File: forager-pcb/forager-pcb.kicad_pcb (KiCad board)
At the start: 2 copper layers, 272.5 x 96.3 mm, 102 parts, among them J1 Conn_01x02_Pin, J2 Conn_01x02_Pin

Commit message: Move out components to edges and clear all traces
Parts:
- moved LCH1 18.0 mm to (-125.0, -28.0)
- moved LCH13 18.0 mm to (-125.0, 6.00)
- moved LCH7 18.0 mm to (-125.0, -11.0)
- moved LU1 18.0 mm to (-125.5, -40.0)
- moved RCH12 18.0 mm to (125.0, -11.0)
- moved RCH18 18.0 mm to (125.0, 6.00)
- moved RCH6 18.0 mm to (125.0, -28.0)
- moved REF** 18.0 mm to (-111.2, -45.8)
- moved REF** 18.0 mm to (111.2, -45.8)
- moved RU1 18.0 mm to (125.5, -40.0)
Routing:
- net /LROW3: track 159.1 -> 0.00 mm
- net /RCOL4: track 156.1 -> 0.00 mm, vias 1 -> 0
- net /LCOL4: track 153.3 -> 0.00 mm, vias 1 -> 0
- net /LROW1: track 136.9 -> 0.00 mm
- net /RCOL3: track 135.8 -> 0.00 mm, vias 1 -> 0
- net /LCOL3: track 133.6 -> 0.00 mm, vias 1 -> 0
- net /RROW2: track 113.4 -> 0.00 mm
- net /RROW3: track 110.5 -> 0.00 mm
- net /LCOL2: track 97.2 -> 0.00 mm, vias 1 -> 0
- net Net-(LD7-A): track 91.4 -> 0.00 mm
- net LBAT: track 90.7 -> 0.00 mm
- net /LROW2: track 84.9 -> 0.00 mm, vias 2 -> 0
- net RBAT: track 83.9 -> 0.00 mm
- net /LCOL1: track 82.1 -> 0.00 mm, vias 1 -> 0
- net /RCOL2: track 76.3 -> 0.00 mm, vias 1 -> 0
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
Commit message: Move in new columns
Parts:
- moved RCH11 124.3 mm to (107.0, -14.6)
- moved RCH17 124.3 mm to (107.0, 1.72)
- moved RCH5 124.3 mm to (107.0, -31.0)
- moved LCH14 122.4 mm to (-107.0, 1.77)
- moved LCH2 122.4 mm to (-107.0, -30.9)
- moved LCH8 122.4 mm to (-107.0, -14.6)
- moved LD14 32.2 mm to (-46.4, 78.2)
- moved LD2 32.2 mm to (-46.4, 71.5)
- moved LD8 32.2 mm to (-46.4, 74.8)
- moved LCH15 1.00 mm to (-89.0, -1.00)
- moved LCH3 1.00 mm to (-89.0, -35.0)
- moved LCH9 1.00 mm to (-89.0, -18.0)
- moved RCH10 1.00 mm to (89.0, -18.0)
- moved RCH16 1.00 mm to (89.0, -1.00)
- moved RCH4 1.00 mm to (89.0, -35.0)
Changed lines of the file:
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@@
 	(footprint "Custom:SW_choc_v1_HS_MBK"
 		(layer "B.Cu")
-		(at 44 92.56 180)
+		(at 107 -14.64 180)
 		(descr "Hotswap footprint for Kailh Choc style switches")
 		(property "Reference" "RCH11"
@@
 	(footprint "Custom:SW_choc_v1_HS_MBK"
 		(layer "B.Cu")
-		(at -89 -34)
+		(at -89 -35)
 		(descr "Hotswap footprint for Kailh Choc style switches")
 		(property "Reference" "LCH3"
@@
 	(footprint "Custom:SW_choc_v1_HS_MBK"
 		(layer "B.Cu")
-		(at -89 -17 180)
+		(at -89 -18 180)
 		(descr "Hotswap footprint for Kailh Choc style switches")
 		(property "Reference" "LCH9"
@@
 	(footprint "Custom:SW_choc_v1_HS_MBK"
 		(layer "B.Cu")
-		(at 89 0)
+		(at 89 -1)
 		(descr "Hotswap footprint for Kailh Choc style switches")
 		(property "Reference" "RCH16"
@@
 	(footprint "Custom:SW_choc_v1_HS_MBK"
 		(layer "B.Cu")
-		(at 89 -17 180)
+		(at 89 -18 180)
 		(descr "Hotswap footprint for Kailh Choc style switches")
 		(property "Reference" "RCH10"
@@
 	(footprint "Diode_SMD:D_SOD-123"
 		(layer "B.Cu")
-		(at -14.35 71.5 180)
+		(at -46.35 74.85 180)
 		(descr "SOD-123")
 		(tags "SOD-123")
@@
 	(footprint "Diode_SMD:D_SOD-123"
 		(layer "B.Cu")
-		(at -14.35 74.85 180)
+		(at -46.35 78.2 180)
 		(descr "SOD-123")
 		(tags "SOD-123")
@@
 	(footprint "Custom:SW_choc_v1_HS_MBK"
 		(layer "B.Cu")
-		(at -89 0)
+		(at -89 -1)
 		(descr "Hotswap footprint for Kailh Choc style switches")
 		(property "Reference" "LCH15"
@@
 	(footprint "Custom:SW_choc_v1_HS_MBK"
 		(layer "B.Cu")
-		(at -33.5 83.28 180)
+		(at -107 -14.59 180)
 		(descr "Hotswap footprint for Kailh Choc style switches")
 		(property "Reference" "LCH8"
@@
 	(footprint "Custom:SW_choc_v1_HS_MBK"
 		(layer "B.Cu")
-		(at -33.5 66.92 180)
+		(at -107 -30.95 180)
 		(descr "Hotswap footprint for Kailh Choc style switches")
 		(property "Reference" "LCH2"
@@
 	(footprint "Custom:SW_choc_v1_HS_MBK"
 		(layer "B.Cu")
-		(at 89 -34 180)
+		(at 89 -35 180)
 		(descr "Hotswap footprint for Kailh Choc style switches")
 		(property "Reference" "RCH4"
@@
 	(footprint "Custom:SW_choc_v1_HS_MBK"
 		(layer "B.Cu")
-		(at -33.5 99.64 180)
+		(at -107 1.77 180)
 		(descr "Hotswap footprint for Kailh Choc style switches")
 		(property "Reference" "LCH14"
@@
 	(footprint "Diode_SMD:D_SOD-123"
 		(layer "B.Cu")
-		(at -14.35 68.15 180)
+		(at -46.35 71.5 180)
 		(descr "SOD-123")
 		(tags "SOD-123")
@@
 	(footprint "Custom:SW_choc_v1_HS_MBK"
 		(layer "B.Cu")
-		(at 44 76.2 180)
+		(at 107 -31 180)
 		(descr "Hotswap footprint for Kailh Choc style switches")
 		(property "Reference" "RCH5"
@@
 	(footprint "Custom:SW_choc_v1_HS_MBK"
 		(layer "B.Cu")
-		(at 44 108.92 180)
+		(at 107 1.72 180)
 		(descr "Hotswap footprint for Kailh Choc style switches")
 		(property "Reference" "RCH17"

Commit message: Set left diodes
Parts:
- moved LD2 117.6 mm to (-50.0, -46.0), turned to -90 degrees
- moved LD8 97.9 mm to (-22.0, -20.0)
- moved LD14 75.8 mm to (-85.0, 13.0), turned to 90 degrees
- moved LD10 3.00 mm to (-22.0, -14.0)
- moved LD11 3.00 mm to (-22.0, -11.0)
- moved LD12 3.00 mm to (-22.0, -8.00)
- moved LD15 3.00 mm to (-82.0, 13.0)
- moved LD3 3.00 mm to (-53.0, -46.0)
- moved LD4 3.00 mm to (-56.0, -46.0)
- moved LD9 3.00 mm to (-22.0, -17.0)
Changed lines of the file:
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@@
 	(footprint "Diode_SMD:D_SOD-123"
 		(layer "B.Cu")
-		(at -85 13 90)
+		(at -82 13 90)
 		(descr "SOD-123")
 		(tags "SOD-123")
@@
 			(at 0 2 0)
 			(layer "B.SilkS")
+			(hide yes)
 			(effects
 				(font
@@
 			(at 0 2 0)
 			(layer "B.SilkS")
+			(hide yes)
 			(effects
 				(font
@@
 	(footprint "Diode_SMD:D_SOD-123"
 		(layer "B.Cu")
-		(at -22 -14 180)
+		(at -22 -11 180)
 		(descr "SOD-123")
 		(tags "SOD-123")
@@
 			(at 0 2 0)
 			(layer "B.SilkS")
+			(hide yes)
 			(effects
 				(font
@@
 	(footprint "Diode_SMD:D_SOD-123"
 		(layer "B.Cu")
-		(at -46.35 74.85 180)
+		(at -22 -20 180)
 		(descr "SOD-123")
 		(tags "SOD-123")
@@
 			(at 0 2 0)
 			(layer "B.SilkS")
+			(hide yes)
 			(effects
 				(font
@@
 	(footprint "Diode_SMD:D_SOD-123"
 		(layer "B.Cu")
-		(at -22 -20 180)
+		(at -22 -17 180)
 		(descr "SOD-123")
 		(tags "SOD-123")
@@
 	(footprint "Diode_SMD:D_SOD-123"
 		(layer "B.Cu")
-		(at -46.35 78.2 180)
+		(at -85 13 90)
 		(descr "SOD-123")
 		(tags "SOD-123")
 		(property "Reference" "LD14"
-			(at 0 2 0)
+			(at 0 2 90)
 			(layer "B.SilkS")
+			(hide yes)
 			(effects
 				(font
@@
 		)
 		(property "Value" "D"
-			(at 0 -2.1 0)
+			(at 0 -2.1 90)
 			(layer "B.Fab")
 			(effects
@@
 		)
 		(property "Footprint" "Diode_SMD:D_SOD-123"
-			(at 0 0 0)
+			(at 0 0 -90)
 			(unlocked yes)
 			(layer "B.Fab")
@@
 		)
 		(property "Datasheet" ""
-			(at 0 0 0)
+			(at 0 0 -90)
 			(unlocked yes)
 			(layer "B.Fab")
@@
 		)
 		(property "Description" "Diode"
-			(at 0 0 0)
+			(at 0 0 -90)
 			(unlocked yes)
 			(layer "B.Fab")
@@
 		)
 		(property "Sim.Device" "D"
-			(at 0 0 0)
+			(at 0 0 -90)
 			(unlocked yes)
 			(layer "B.Fab")
@@
 		)
 		(property "Sim.Pins" "1=K 2=A"
-			(at 0 0 0)
+			(at 0 0 -90)
 			(unlocked yes)
 			(layer "B.Fab")
@@
 		(attr smd)
 		(fp_line
-			(start 1.65 1)
-			(end -2.36 1)
-			(stroke
-				(width 0.12)
-				(type solid)
-			)
-			(layer "B.SilkS")
-		)
-		(fp_line
 			(start 1.65 -1)
 			(end -2.36 -1)
@@
 		)
 		(fp_line
-			(start 2.35 1.15)
-			(end -2.35 1.15)
+			(start 1.65 1)
+			(end -2.36 1)
 			(stroke
-				(width 0.05)
+				(width 0.12)
 				(type solid)
 			)
-			(layer "B.CrtYd")
+			(layer "B.SilkS")
 		)
 		(fp_line
@@
 		)
 		(fp_line
-			(start 1.4 0.9)
-			(end -1.4 0.9)
+			(start 2.35 1.15)
+			(end -2.35 1.15)
 			(stroke
-				(width 0.1)
+				(width 0.05)
 				(type solid)
 			)
-			(layer "B.Fab")
+			(layer "B.CrtYd")
 		)
 		(fp_line
@@
 		)
 		(fp_line
-			(start 0.75 0)
-			(end 0.25 0)
+			(start -1.4 -0.9)
+			(end 1.4 -0.9)
 			(stroke
 				(width 0.1)
@@
 		)
 		(fp_line
-			(start 0.25 0.4)
+			(start -0.35 -0.55)
 			(end -0.35 0)
 			(stroke
@@
 		)
 		(fp_line
-			(start -0.35 0.55)
-			(end -0.35 0)
+			(start 0.75 0)
+			(end 0.25 0)
 			(stroke
 				(width 0.1)
@@
 		)
 		(fp_line
-			(start -0.35 -0.55)
+			(start 0.25 0.4)
 			(end -0.35 0)
 			(stroke
@@
 		)
 		(fp_line
-			(start -1.4 0.9)
-			(end -1.4 -0.9)
+			(start -0.35 0.55)
+			(end -0.35 0)
 			(stroke
 				(width 0.1)
@@
 		)
 		(fp_line
-			(start -1.4 -0.9)
-			(end 1.4 -0.9)
+			(start 1.4 0.9)
+			(end -1.4 0.9)
+			(stroke
+				(width 0.1)
+				(type solid)
+			)
+			(layer "B.Fab")
+		)
+		(fp_line
+			(start -1.4 0.9)
+			(end -1.4 -0.9)
 			(stroke
 				(width 0.1)
@@
 		)
 		(fp_text user "${REFERENCE}"
-			(at 0 2 0)
+			(at 0 2 90)
 			(layer "B.Fab")
 			(effects
@@
 		)
 		(pad "1" smd roundrect
-			(at -1.65 0 180)
+			(at -1.65 0 90)
 			(size 0.9 1.2)
 			(layers "B.Cu" "B.Paste" "B.Mask")
@@
 		)
 		(pad "2" smd roundrect
-			(at 1.65 0 180)
+			(at 1.65 0 90)
 			(size 0.9 1.2)
 			(layers "B.Cu" "B.Paste" "B.Mask")
@@
 	(footprint "Diode_SMD:D_SOD-123"
 		(layer "B.Cu")
-		(at -50 -46 -90)
+		(at -53 -46 -90)
 		(descr "SOD-123")
 		(tags "SOD-123")
@@
 	(footprint "Diode_SMD:D_SOD-123"
 		(layer "B.Cu")
-		(at -22 -17 180)
+		(at -22 -14 180)
 		(descr "SOD-123")
 		(tags "SOD-123")
@@
 	(footprint "Diode_SMD:D_SOD-123"
 		(layer "B.Cu")
-		(at -46.35 71.5 180)
+		(at -50 -46 -90)
 		(descr "SOD-123")
 		(tags "SOD-123")
 		(property "Reference" "LD2"
-			(at 0 2 0)
+			(at 0 2 90)
 			(layer "B.SilkS")
+			(hide yes)
 			(effects
 				(font
@@
 		)
 		(property "Value" "D"
-			(at 0 -2.1 0)
+			(at 0 -2.1 90)
 			(layer "B.Fab")
 			(effects
@@
 		)
 		(property "Footprint" "Diode_SMD:D_SOD-123"
-			(at 0 0 0)
+			(at 0 0 90)
 			(unlocked yes)
 			(layer "B.Fab")
@@
 		)
 		(property "Datasheet" ""
-			(at 0 0 0)
+			(at 0 0 90)
 			(unlocked yes)
 			(layer "B.Fab")
@@
 		)
 		(property "Description" "Diode"
-			(at 0 0 0)
+			(at 0 0 90)
 			(unlocked yes)
 			(layer "B.Fab")
@@
 		)
 		(property "Sim.Device" "D"
-			(at 0 0 0)
+			(at 0 0 90)
 			(unlocked yes)
 			(layer "B.Fab")
@@
 		)
 		(property "Sim.Pins" "1=K 2=A"
-			(at 0 0 0)
+			(at 0 0 90)
 			(unlocked yes)
 			(layer "B.Fab")
@@
 		)
 		(fp_line
-			(start 1.65 -1)
-			(end -2.36 -1)
+			(start -2.36 -1)
+			(end -2.36 1)
 			(stroke
 				(width 0.12)
@@
 		)
 		(fp_line
-			(start -2.36 -1)
-			(end -2.36 1)
+			(start 1.65 -1)
+			(end -2.36 -1)
 			(stroke
 				(width 0.12)
@@
 		)
 		(fp_line
-			(start 2.35 -1.15)
-			(end 2.35 1.15)
+			(start -2.35 -1.15)
+			(end -2.35 1.15)
 			(stroke
 				(width 0.05)
@@
 		)
 		(fp_line
-			(start -2.35 -1.15)
-			(end -2.35 1.15)
+			(start 2.35 -1.15)
+			(end 2.35 1.15)
 			(stroke
 				(width 0.05)
@@
 		)
 		(fp_line
-			(start 1.4 0.9)
-			(end -1.4 0.9)
+			(start -1.4 0.9)
+			(end -1.4 -0.9)
 			(stroke
 				(width 0.1)
@@
 		)
 		(fp_line
-			(start 1.4 -0.9)
-			(end 1.4 0.9)
+			(start 1.4 0.9)
+			(end -1.4 0.9)
 			(stroke
 				(width 0.1)
@@
 		)
 		(fp_line
-			(start 0.75 0)
-			(end 0.25 0)
+			(start -0.35 0.55)
+			(end -0.35 0)
 			(stroke
 				(width 0.1)
@@
 		)
 		(fp_line
-			(start 0.25 -0.4)
-			(end 0.25 0.4)
+			(start -0.35 0)
+			(end -0.75 0)
 			(stroke
 				(width 0.1)
@@
 		)
 		(fp_line
-			(start -0.35 0.55)
-			(end -0.35 0)
+			(start -0.35 0)
+			(end 0.25 -0.4)
 			(stroke
 				(width 0.1)
@@
 		)
 		(fp_line
-			(start -0.35 0)
-			(end 0.25 -0.4)
+			(start 0.75 0)
+			(end 0.25 0)
 			(stroke
 				(width 0.1)
@@
 		)
 		(fp_line
-			(start -0.35 0)
-			(end -0.75 0)
+			(start 0.25 -0.4)
+			(end 0.25 0.4)
 			(stroke
 				(width 0.1)
@@
 		)
 		(fp_line
-			(start -1.4 0.9)
-			(end -1.4 -0.9)
+			(start -1.4 -0.9)
+			(end 1.4 -0.9)
 			(stroke
 				(width 0.1)
@@
 		)
 		(fp_line
-			(start -1.4 -0.9)
-			(end 1.4 -0.9)
+			(start 1.4 -0.9)
+			(end 1.4 0.9)
 			(stroke
 				(width 0.1)
@@
 		)
 		(fp_text user "${REFERENCE}"
-			(at 0 2 0)
+			(at 0 2 90)
 			(layer "B.Fab")
 			(effects
@@
 		)
 		(pad "1" smd roundrect
-			(at -1.65 0 180)
+			(at -1.65 0 270)
 			(size 0.9 1.2)
 			(layers "B.Cu" "B.Paste" "B.Mask")
@@
 		)
 		(pad "2" smd roundrect
-			(at 1.65 0 180)
+			(at 1.65 0 270)
 			(size 0.9 1.2)
 			(layers "B.Cu" "B.Paste" "B.Mask")
@@
 	(footprint "Diode_SMD:D_SOD-123"
 		(layer "B.Cu")
-		(at -53 -46 -90)
+		(at -56 -46 -90)
 		(descr "SOD-123")
 		(tags "SOD-123")
@@
 	(footprint "Diode_SMD:D_SOD-123"
 		(layer "B.Cu")
-		(at -22 -11 180)
+		(at -22 -8 180)
 		(descr "SOD-123")
 		(tags "SOD-123")

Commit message: Fix bad annotation
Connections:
- LCH10 pad 1: /LCOL2 -> /LCOL3
- LCH11 pad 1: /LCOL3 -> /LCOL4
- LCH12 pad 1: /LCOL4 -> /LCOL5
- LCH14 pad 1: /LCOL0 -> /LCOL1
- LCH15 pad 1: /LCOL1 -> /LCOL2
- LCH16 pad 1: /LCOL2 -> /LCOL3
- LCH17 pad 1: /LCOL3 -> /LCOL4
- LCH18 pad 1: /LCOL4 -> /LCOL5
- LCH19 pad 1: /LCOL3 -> /LCOL4
- LCH2 pad 1: /LCOL0 -> /LCOL1
- LCH20 pad 1: /LCOL4 -> /LCOL5
- LCH3 pad 1: /LCOL1 -> /LCOL2
- LCH4 pad 1: /LCOL2 -> /LCOL3
- LCH5 pad 1: /LCOL3 -> /LCOL4
- LCH6 pad 1: /LCOL4 -> /LCOL5
- LCH8 pad 1: /LCOL0 -> /LCOL1
- LCH9 pad 1: /LCOL1 -> /LCOL2
- LU1 pad 6: unconnected-(LU1-P0.05/5-Pad6) -> /LCOL5
- RCH1 pad 1: /RCOL4 -> /RCOL5
- RCH10 pad 1: /RCOL1 -> /RCOL2
- RCH11 pad 1: /RCOL0 -> /RCOL1
- RCH13 pad 1: /RCOL4 -> /RCOL5
- RCH14 pad 1: /RCOL3 -> /RCOL4
- RCH15 pad 1: /RCOL2 -> /RCOL3
- RCH16 pad 1: /RCOL1 -> /RCOL2
- RCH17 pad 1: /RCOL0 -> /RCOL1
- RCH19 pad 1: /RCOL4 -> /RCOL5
- RCH2 pad 1: /RCOL3 -> /RCOL4
- RCH20 pad 1: /RCOL3 -> /RCOL4
- RCH3 pad 1: /RCOL2 -> /RCOL3
- RCH4 pad 1: /RCOL1 -> /RCOL2
- RCH5 pad 1: /RCOL0 -> /RCOL1
- RCH7 pad 1: /RCOL4 -> /RCOL5
- RCH8 pad 1: /RCOL3 -> /RCOL4
- RCH9 pad 1: /RCOL2 -> /RCOL3
- RU1 pad 11: /RCOL3 -> /RCOL4
- RU1 pad 12: /RCOL4 -> /RCOL5
- RU1 pad 6: unconnected-(RU1-P0.05/5-Pad6) -> /RCOL3

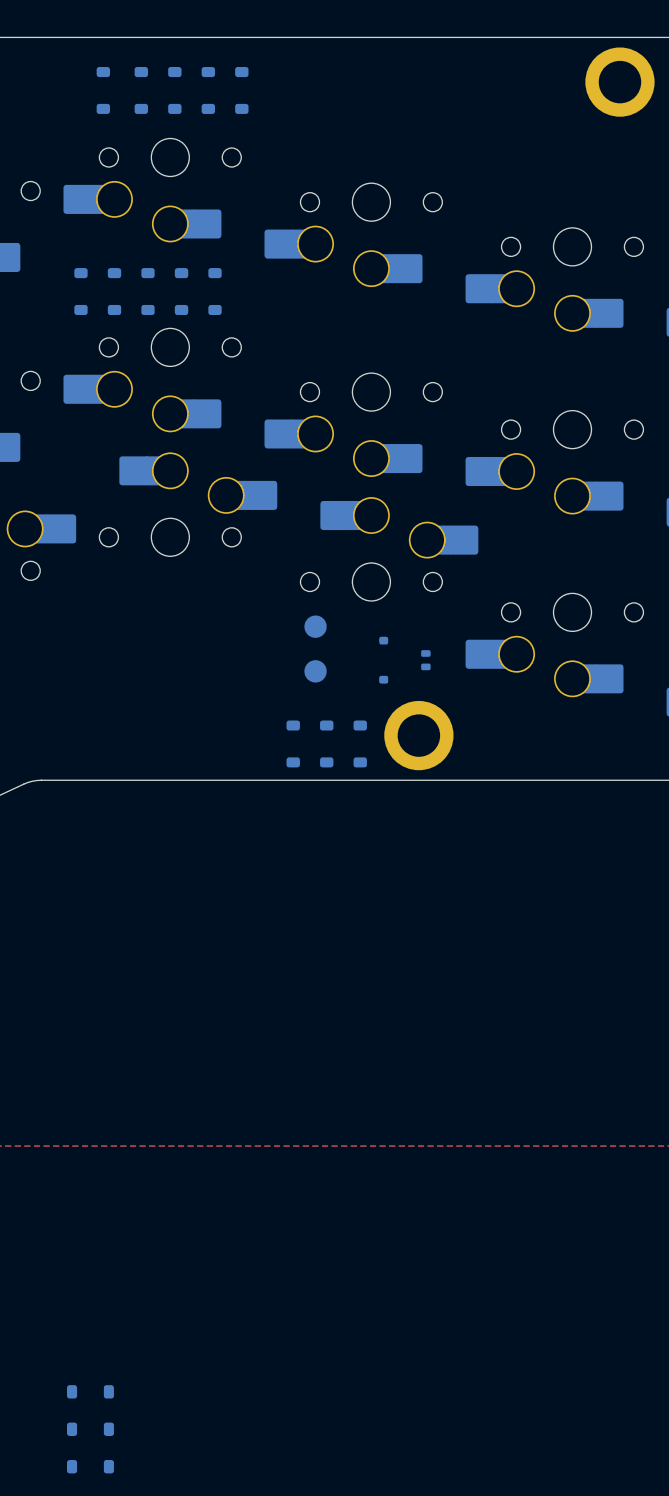
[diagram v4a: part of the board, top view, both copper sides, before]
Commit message: Set right diodes
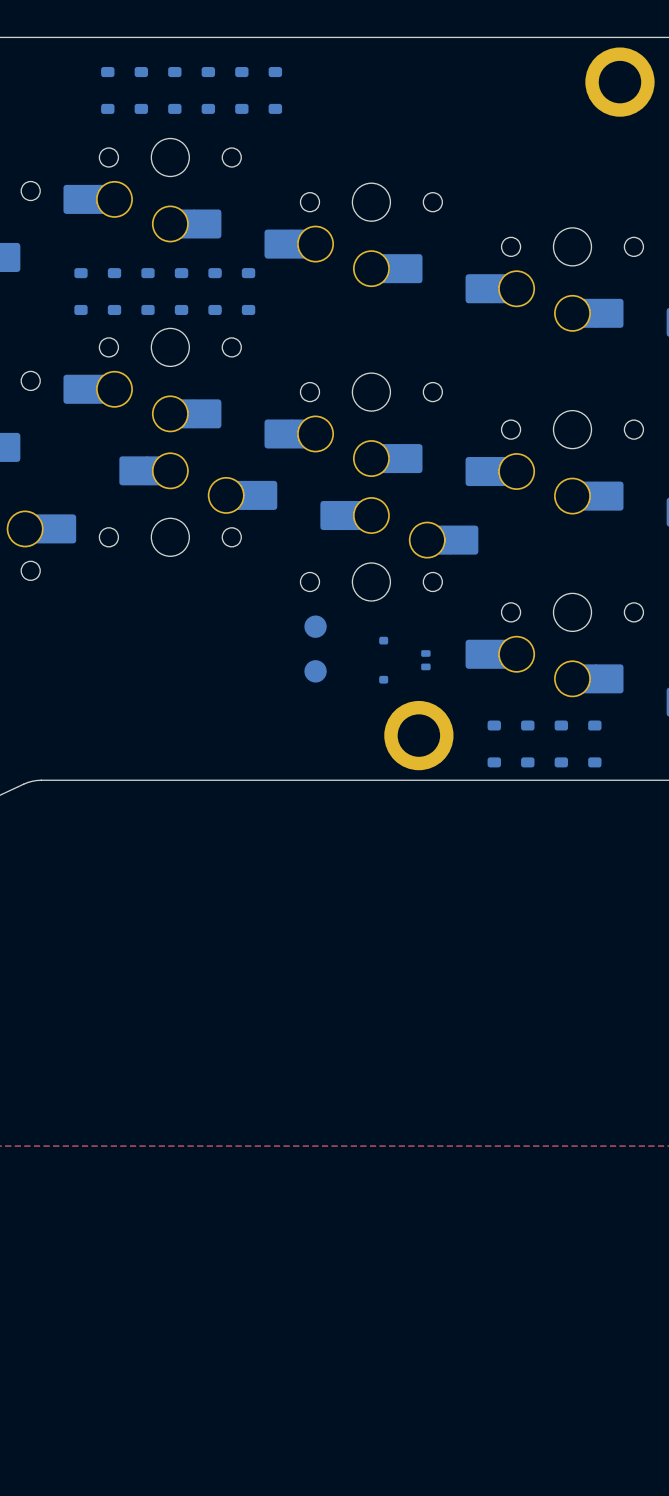
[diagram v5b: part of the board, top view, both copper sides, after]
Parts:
- moved RD5 117.3 mm to (77.4, -45.0), turned to -90 degrees
- moved RD11 102.5 mm to (75.0, -27.0), turned to -90 degrees
- moved RD17 77.2 mm to (106.0, 13.5), turned to 90 degrees
- moved RD18 21.0 mm to (109.0, 13.5)
- moved RD15 18.0 mm to (100.0, 13.5)
- moved RD16 18.0 mm to (103.0, 13.5)
- moved RD12 3.00 mm to (78.0, -27.0)
- moved RD6 3.00 mm to (80.4, -45.0)
- moved RD1 0.40 mm to (65.4, -45.0)

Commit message: Swap to choc v2 comparible centerhole
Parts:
- LCH1, LCH10, LCH11, LCH12, LCH13, LCH14, LCH15, LCH16, LCH17, LCH18, LCH19, LCH2, LCH20, LCH3, LCH4, LCH5, LCH6, LCH7, LCH8, LCH9, RCH1, RCH10, RCH11, RCH12, RCH13, RCH14, RCH15, RCH16, RCH17, RCH18, RCH19, RCH2, RCH20, RCH3, RCH4, RCH5, RCH6, RCH7, RCH8, RCH9: footprint Custom:SW_choc_v1_HS_MBK -> Custom:SW_choc_v1v2_HS_MBK

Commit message: Swap to solder sockets
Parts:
- LCH1, LCH10, LCH11, LCH12, LCH13, LCH14, LCH15, LCH16, LCH17, LCH18, LCH19, LCH2, LCH20, LCH3, LCH4, LCH5, LCH6, LCH7, LCH8, LCH9, RCH1, RCH10, RCH11, RCH12, RCH13, RCH14, RCH15, RCH16, RCH17, RCH18, RCH19, RCH2, RCH20, RCH3, RCH4, RCH5, RCH6, RCH7, RCH8, RCH9: footprint Custom:SW_choc_v1v2_HS_MBK -> Custom:Choc_v2_PG1353_socket
